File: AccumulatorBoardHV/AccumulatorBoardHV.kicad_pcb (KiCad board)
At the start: 2 copper layers, 42 parts, among them J1 TS -> GLV Regulator Jumper, J2 To LV Board, J3 Batt Voltage, J4 TS (Switched), J5 IMD TS, J6 To LV Board, J7 Acc LED 1, J8 Acc LED 2, J9 Charger Current, U1 V110C12E100BL, U2 DK1A1B-12V, U3 RDD08110S3V3, U4 PS2501-4, U5 G2RL-1A-E, U6 G2RL-1A-E

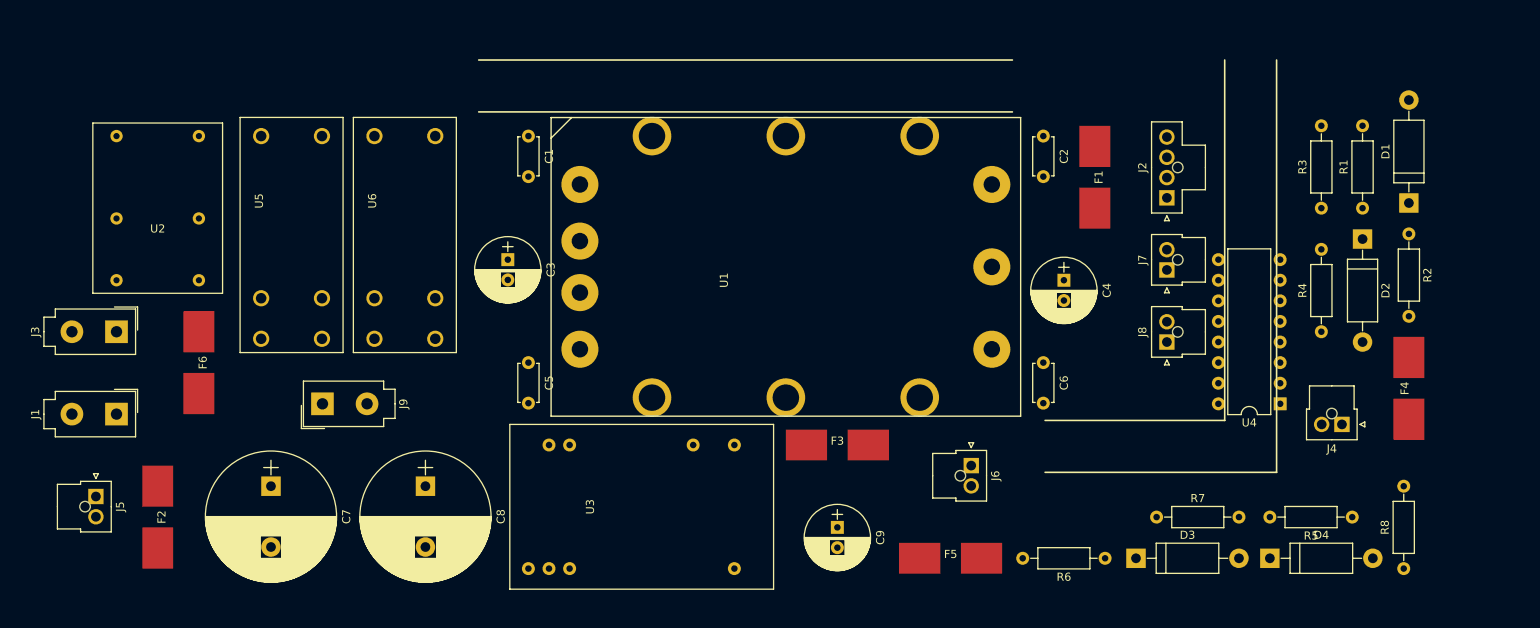
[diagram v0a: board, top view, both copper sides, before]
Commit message: Work for preparation for autorouting
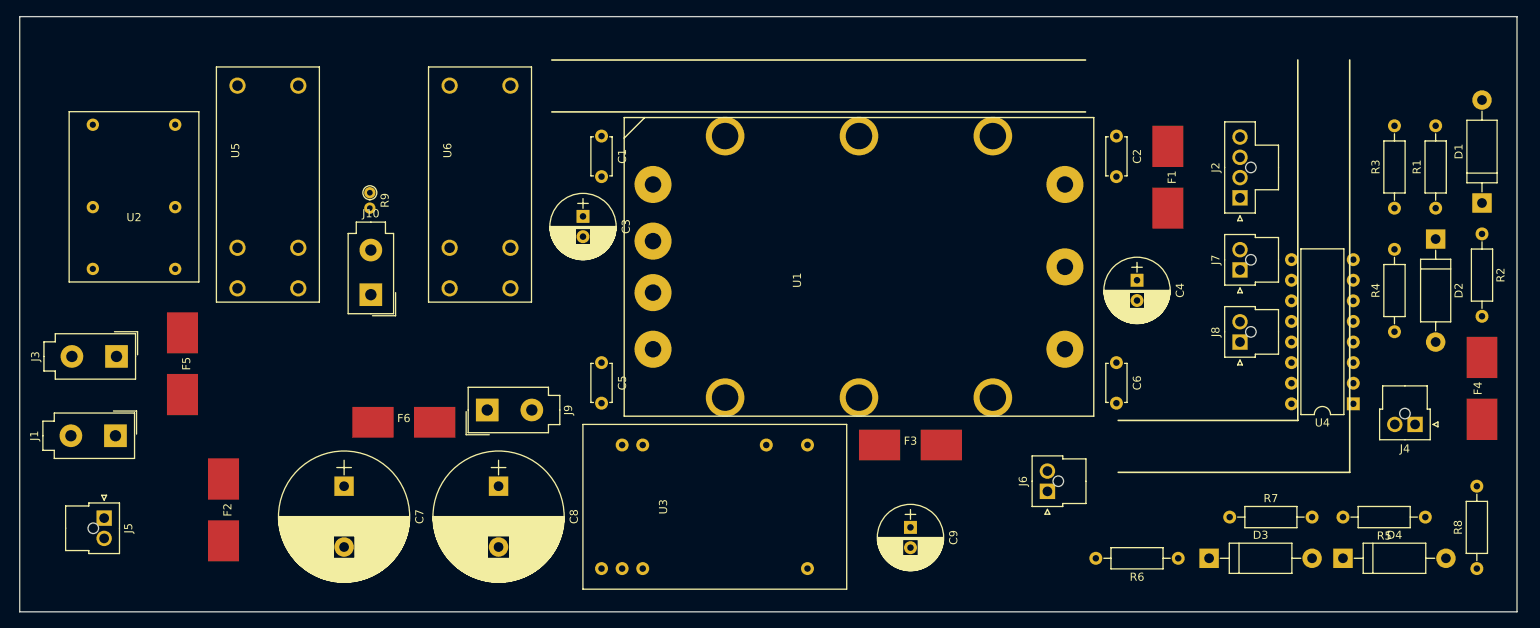
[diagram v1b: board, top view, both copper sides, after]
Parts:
- added J10: Charger Current, Connectors_Molex:Molex_MiniFit-JR-5556-02A_2x01x4.20mm_Straight, F.Cu at (61.8, 62.7)
- added R9: 0, Resistors_THT:R_Axial_DIN0204_L3.6mm_D1.6mm_P1.90mm_Vertical, F.Cu at (61.7, 50.2)
- J9: value Charger Current -> Charger Current to Batt
- moved F5 97.7 mm to (38.6, 71.2), turned to 90 degrees
- moved F6 26.3 mm to (65.9, 78.5), turned to 180 degrees
- moved J9 20.3 mm to (76.2, 77.0)
- moved U6 11.2 mm to (75.3, 37.0)
- moved C3 10.7 mm to (88.0, 53.1)
- moved J6 9.92 mm to (145.3, 87.0), turned to 90 degrees
- moved R8 9.02 mm to (198.2, 96.5)
- moved U1 9.02 mm to (96.6, 43.2)
- moved C1 9.02 mm to (90.3, 43.2)
- moved C2 9.02 mm to (153.8, 43.2)
- moved C4 9.02 mm to (156.3, 61.0)
- moved C5 9.02 mm to (90.3, 71.1)
- moved C6 9.02 mm to (153.8, 71.1)
- moved C7 9.02 mm to (58.5, 86.4)
- moved C8 9.02 mm to (77.6, 86.4)
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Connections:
- net Net-(F6-Pad2) renamed /BATT+_CHGFUSED
- F6 pad 1: /BATT+_DIRECT -> /BATT+_CHARGER
- J9 pad 1: /CHARGER+ -> /BATT+_CHARGER
- J9 pad 2: /CHARGER- -> /BATT-_CHARGER
- R8 pad 2: /CHARGER- -> Net-(R8-Pad2)
- U6 pad 3: /BATT- -> /BATT-_CHARGER
- U6 pad 5: /BATT- -> /BATT-_CHARGER
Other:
- board outline added: 184.7 x 73.4 mm
- net class BattCurrent added: clearance 0.2, trace_width 0.5, via_dia 1.2, via_drill 0.4
- net class ChgCurrent added: clearance 0.2, trace_width 4, via_dia 3.2, via_drill 2

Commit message: Autoroute AccumulatorHV PCB
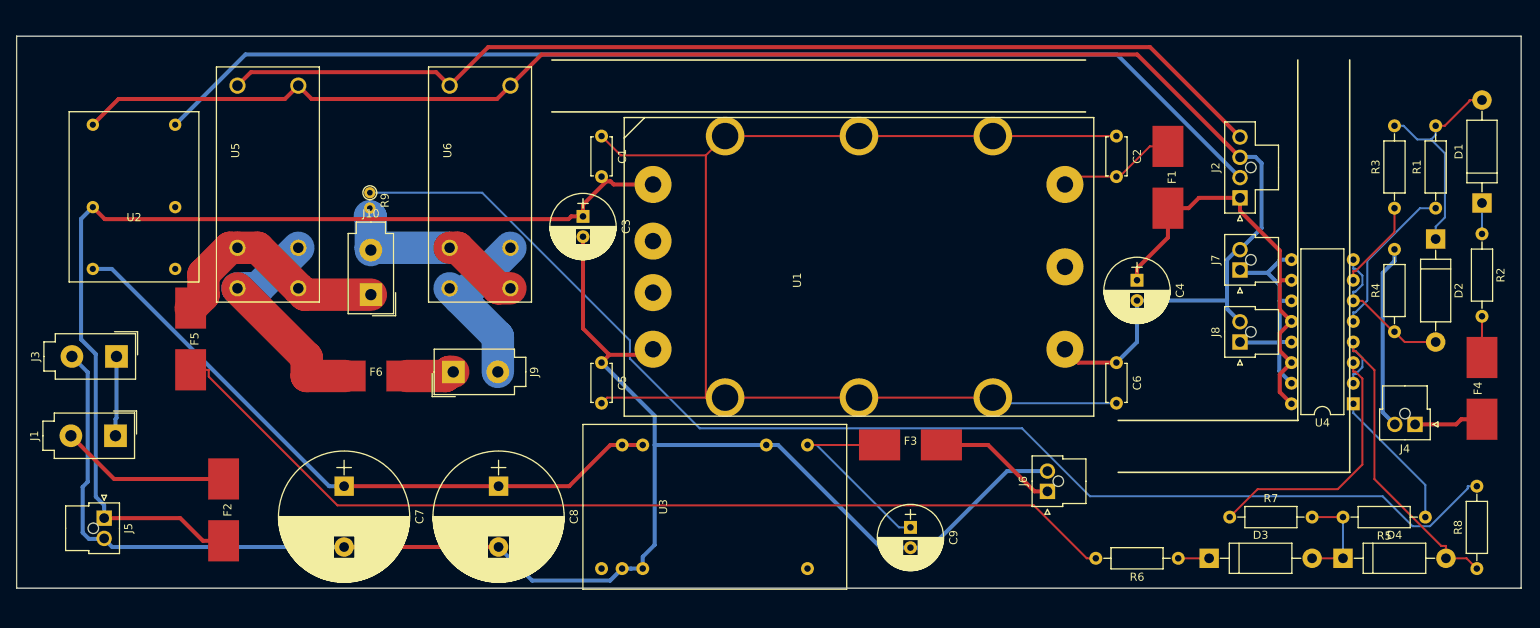
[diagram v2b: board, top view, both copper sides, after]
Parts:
- moved F6 6.66 mm to (62.5, 72.8)
- moved J9 6.30 mm to (72.0, 72.3)
- moved F5 3.21 mm to (39.6, 68.2)
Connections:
- net Net-(F2-Pad2) renamed /BATT+_DIRFUSED
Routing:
- net /BATT-: track 0.00 -> 204.3 mm
- net GND: track 0.00 -> 203.7 mm
- net Net-(C1-Pad1): track 0.00 -> 159.4 mm
- net Net-(R8-Pad2): track 0.00 -> 157.1 mm
- net /12V: track 0.00 -> 141.2 mm
- net /AIRS_FINAL_CHARGER: track 0.00 -> 131.6 mm
- net /BATT+: track 0.00 -> 129.5 mm
- net Net-(F5-Pad1): track 0.00 -> 121.7 mm
- net /BATT+_LVBOARD: track 0.00 -> 81.0 mm
- net /12V_SRC: track 0.00 -> 51.8 mm
- net Net-(D4-Pad2): track 0.00 -> 42.6 mm
- net Net-(R7-Pad1): track 0.00 -> 32.2 mm
- net /12V_INDICATOR: track 0.00 -> 29.9 mm
- net /CHARGER+: track 0.00 -> 29.2 mm
- net /BATT+_CHGFUSED: track 0.00 -> 28.7 mm
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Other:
- board size 184.7 x 73.4 mm -> 185.5 x 68.1 mm
- net class BattCurrent: clearance 0.2 -> 0.4
- net class Default: via_dia 0.6 -> 0.8

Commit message: Revise Accumulator HV and LV, route Dash Switchbox, begin PE HV
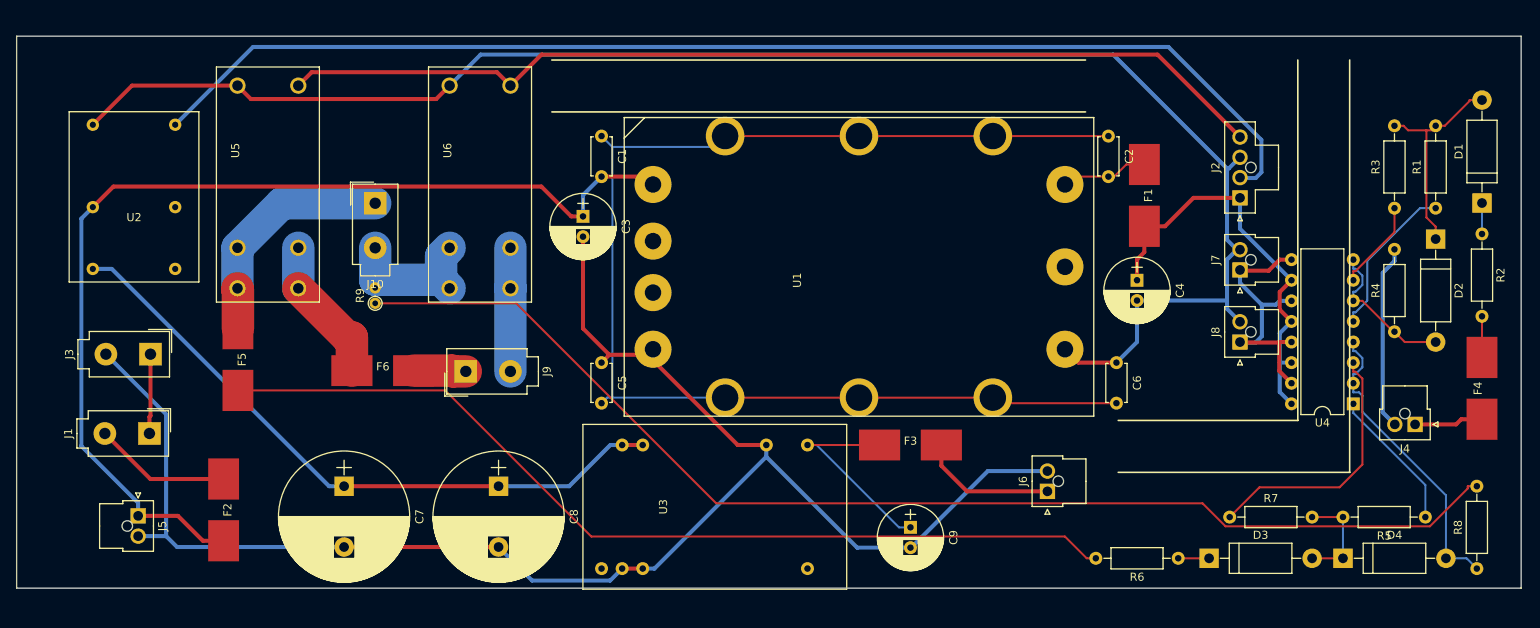
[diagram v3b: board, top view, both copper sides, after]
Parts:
- moved R9 13.7 mm to (62.4, 63.8), turned to 90 degrees
- moved J10 11.3 mm to (62.4, 51.5), turned to 0 degrees
- moved F5 6.36 mm to (45.5, 70.7)
- moved J3 4.20 mm to (34.7, 70.1)
- moved J5 4.20 mm to (33.1, 90.0)
- moved J1 4.20 mm to (34.5, 79.9)
- moved F1 3.67 mm to (157.2, 50.5)
- moved J9 1.55 mm to (73.6, 72.2)
- moved F6 1.07 mm to (63.3, 72.1)
- moved C2 0.99 mm to (152.8, 43.2)
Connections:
- U5 pad 1: GND -> /AIRS_FINAL_CHARGER
- U5 pad 4: /CHARGER+ -> /BATT+_CHGFUSED
- U5 pad 5: /BATT+_CHGFUSED -> /CHARGER+
- U5 pad 8: /AIRS_FINAL_CHARGER -> GND
- U6 pad 1: GND -> /AIRS_FINAL_CHARGER
- U6 pad 4: /CHARGER- -> /BATT-_CHARGER
- U6 pad 5: /BATT-_CHARGER -> /CHARGER-
- U6 pad 8: /AIRS_FINAL_CHARGER -> GND
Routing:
- net /BATT+_CHGFUSED: track 28.7 -> 18.2 mm
- net /12V: track 141.2 -> 149.6 mm
- net /AIRS_FINAL_CHARGER: track 131.6 -> 123.3 mm
- net Net-(R8-Pad2): track 157.1 -> 149.5 mm
- net Net-(F5-Pad1): track 121.7 -> 114.4 mm
- net /BATT-_CHARGER: track 21.6 -> 15.2 mm
- net /BATT-: track 204.3 -> 198.5 mm
- net /CHARGER-: track 24.5 -> 18.9 mm
- net /12V_INDICATOR: track 29.9 -> 35.2 mm
- net Net-(D4-Pad2): track 42.6 -> 37.4 mm
- net /BATT+_DIRFUSED: track 21.0 -> 17.0 mm
- net Net-(C2-Pad2): track 14.6 -> 10.8 mm
- net GND: track 203.7 -> 200.6 mm
- net /3.3V_TS: track 15.4 -> 16.9 mm
- net Net-(D1-Pad2): track 27.7 -> 26.9 mm
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
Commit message: Tweak AccumulatorHV PCB
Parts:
- moved F1 6.91 mm to (163.2, 47.0)
- moved C4 3.53 mm to (158.5, 58.2)
- moved J6 0.89 mm to (144.4, 87.0)
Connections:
- C2 pad 2: Net-(C2-Pad2) -> /VICOR_OUT
- C4 pad 1: /12V_SRC -> /VICOR_OUT
- F1 pad 2: Net-(C2-Pad2) -> /VICOR_OUT
- U1 pad 7: Net-(C2-Pad2) -> /VICOR_OUT
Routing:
- net /VICOR_OUT: track 0.00 -> 29.4 mm
- net /12V_SRC: track 52.2 -> 38.0 mm
- net Net-(C2-Pad2): track 10.8 -> 0.00 mm
- net /12V_INDICATOR: track 35.2 -> 29.9 mm
- net /BATT-: track 198.5 -> 196.6 mm
- net /3.3V_TS: track 16.9 -> 16.1 mm
- net GND: track 200.6 -> 201.2 mm

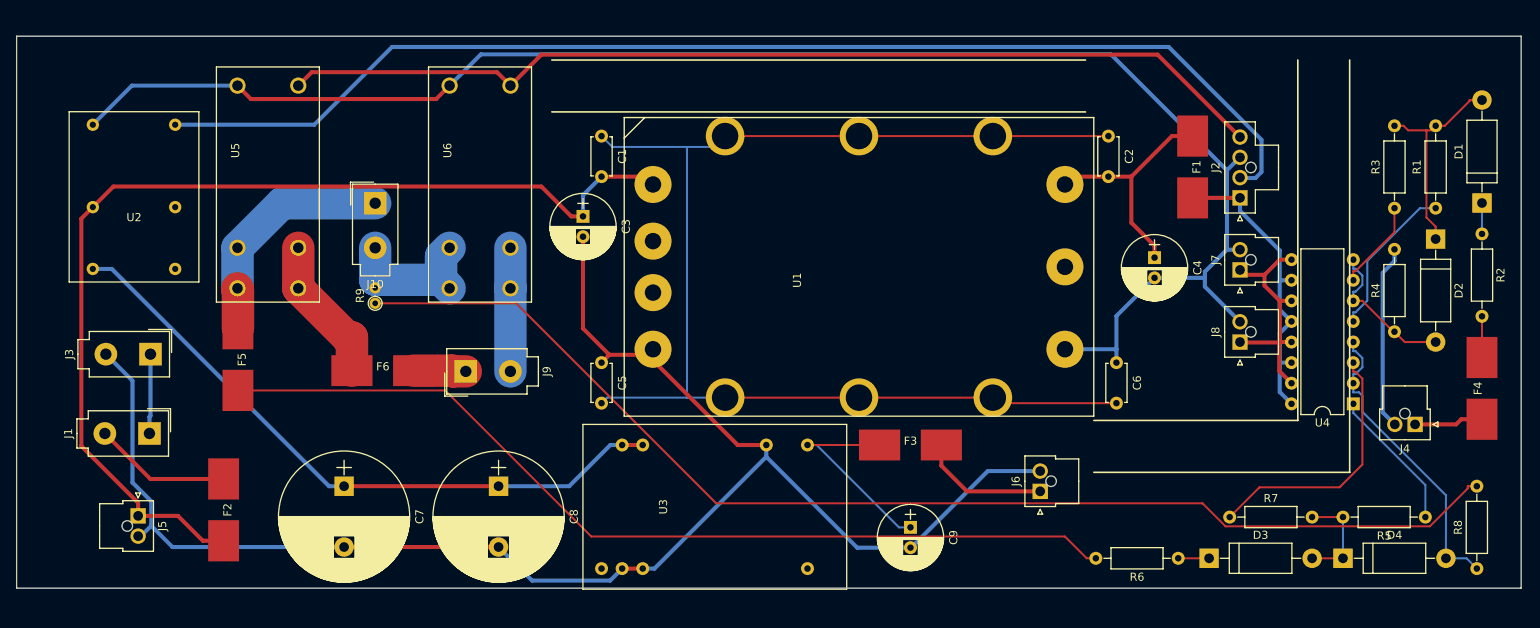
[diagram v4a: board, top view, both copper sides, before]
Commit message: Add mounting holes to Accumulator HV PCB
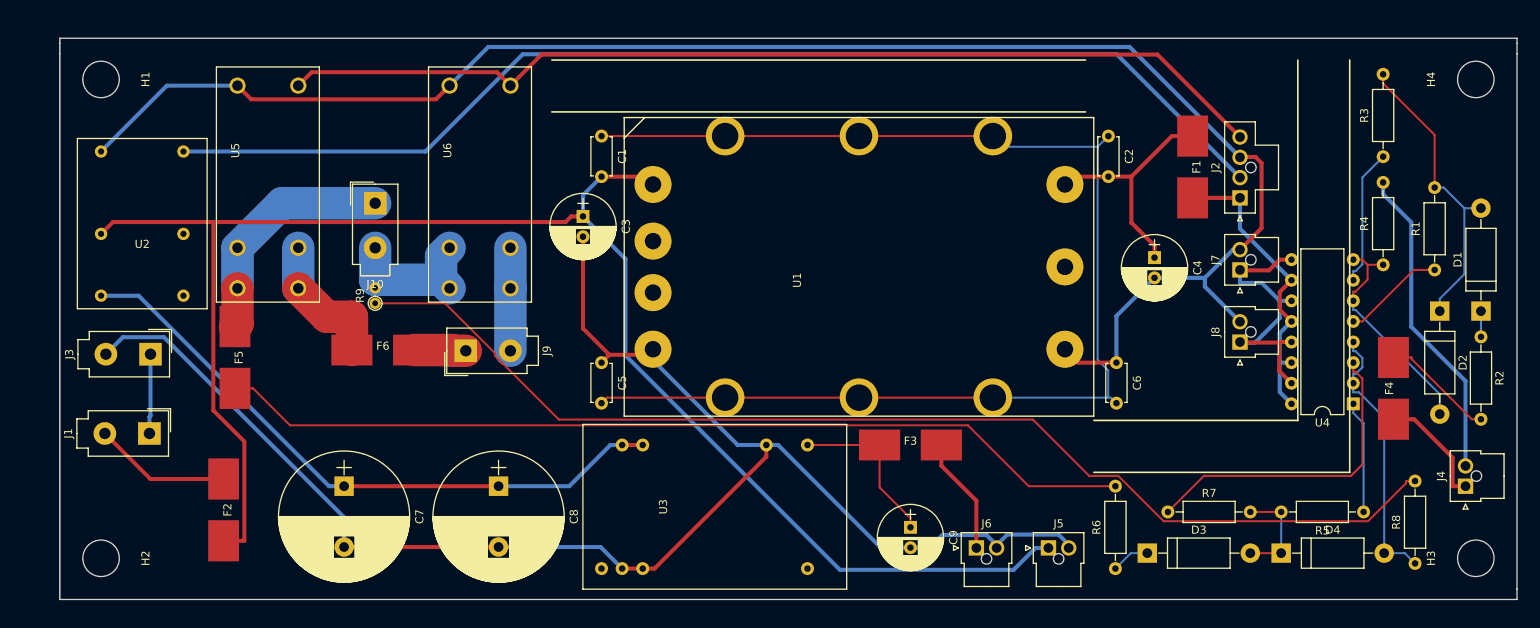
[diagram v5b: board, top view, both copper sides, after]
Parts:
- added H1: MtngHole, Mounting_Holes:MountingHole_4.5mm, F.Cu at (28.6, 36.2)
- added H2: MtngHole, Mounting_Holes:MountingHole_4.5mm, F.Cu at (28.6, 95.2)
- added H3: MtngHole, Mounting_Holes:MountingHole_4.5mm, F.Cu at (198.1, 95.2)
- added H4: MtngHole, Mounting_Holes:MountingHole_4.5mm, F.Cu at (198.1, 36.2)
- moved J5 112.3 mm to (145.4, 94.0), turned to 0 degrees
- moved D1 13.3 mm to (198.8, 64.8)
- moved R2 12.7 mm to (198.8, 67.9)
- moved F4 10.9 mm to (188.0, 74.3)
- moved J6 10.5 mm to (136.5, 94.0), turned to 0 degrees
- moved J4 9.84 mm to (196.8, 86.4), turned to 90 degrees
- moved D2 8.90 mm to (193.7, 64.8)
- moved R4 8.37 mm to (186.7, 59.1)
- moved R6 7.85 mm to (153.7, 96.5), turned to 90 degrees
- moved D3 7.65 mm to (157.6, 94.6)
- moved D4 7.65 mm to (174.1, 94.6)
- moved R5 7.65 mm to (184.3, 89.5)
- moved R7 7.65 mm to (160.1, 89.5)
- moved R8 7.65 mm to (190.6, 95.9)
- moved R1 7.62 mm to (193.0, 59.7)
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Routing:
- net /BATT+: track 129.0 -> 199.9 mm
- net /TS-: track 22.8 -> 39.2 mm
- net Net-(D1-Pad2): track 26.9 -> 37.3 mm
- net Net-(D2-Pad2): track 18.6 -> 27.8 mm
- net Net-(F4-Pad1): track 5.08 -> 14.1 mm
- net /12V: track 149.6 -> 141.6 mm
- net Net-(R8-Pad2): track 149.5 -> 141.8 mm
- net Net-(R7-Pad1): track 32.2 -> 39.6 mm
- net Net-(R1-Pad1): track 19.5 -> 12.7 mm
- net /12V_INDICATOR: track 29.9 -> 36.1 mm
- net /TS+: track 8.52 -> 14.4 mm
- net Net-(R3-Pad1): track 11.2 -> 16.9 mm
- net Net-(C9-Pad1): track 25.8 -> 20.6 mm
- net GND: track 201.2 -> 206.2 mm
- net /BATT-: track 196.6 -> 191.6 mm
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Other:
- board size 185.5 x 68.1 mm -> 179.7 x 69.2 mm

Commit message: Add larger fuse to AccumulatorHV board
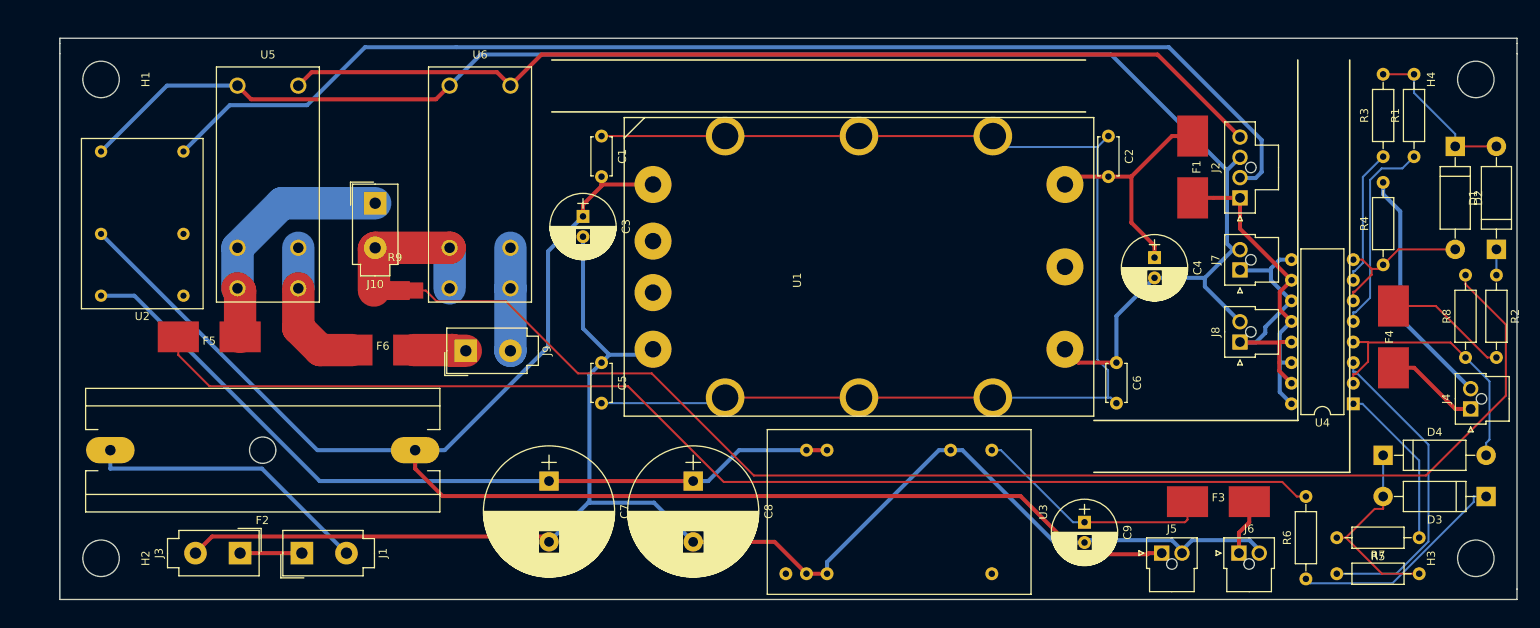
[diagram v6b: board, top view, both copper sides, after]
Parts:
- F2: footprint FSFootprints:SMD Fuse -> Fuse_Holders_and_Fuses:Fuseholder6x32_Horiz_Open_Schurter0031-8002
- R9: footprint Resistors_THT:R_Axial_DIN0204_L3.6mm_D1.6mm_P1.90mm_Vertical -> Oddities:NetTie-I_Connected_SMD
- moved D3 42.4 mm to (199.4, 87.6), turned to 180 degrees
- moved F3 38.6 mm to (166.4, 88.3)
- moved J6 32.4 mm to (168.9, 94.6)
- moved J3 26.9 mm to (45.7, 94.6)
- moved R8 26.2 mm to (196.8, 70.5)
- moved C7 25.3 mm to (83.8, 85.7)
- moved F2 24.7 mm to (67.3, 81.9), turned to 180 degrees
- moved C8 24.0 mm to (101.6, 85.7)
- moved J1 23.9 mm to (53.3, 94.6), turned to 90 degrees
- moved R6 23.5 mm to (177.2, 97.8)
- moved U3 22.7 mm to (113.0, 97.2)
- moved R7 22.2 mm to (181.0, 97.2)
- moved C9 21.5 mm to (149.9, 90.8)
- moved D2 20.4 mm to (195.6, 44.5)
- moved D4 17.4 mm to (186.7, 82.5)
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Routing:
- net Net-(F5-Pad1): track 113.6 -> 148.5 mm
- net Net-(R8-Pad2): track 141.8 -> 165.0 mm
- net Net-(D3-Pad1): track 4.73 -> 27.3 mm
- net /BATT+_LVBOARD: track 78.6 -> 100.6 mm
- net /BATT+_DIRFUSED: track 17.0 -> 35.7 mm
- net Net-(D1-Pad2): track 37.3 -> 19.9 mm
- net Net-(R1-Pad1): track 12.7 -> 25.1 mm
- net Net-(D3-Pad2): track 12.7 -> 24.7 mm
- net Net-(C9-Pad1): track 20.6 -> 30.2 mm
- net /TS-: track 39.2 -> 29.9 mm
- net Net-(D2-Pad2): track 27.8 -> 19.0 mm
- net /12V: track 141.6 -> 150.0 mm
- net /3.3V_TS: track 14.5 -> 6.88 mm
- net Net-(R5-Pad1): track 13.9 -> 20.5 mm
- net GND: track 206.2 -> 202.1 mm
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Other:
- net class BattCurrent: via_drill 0.4 -> 0.6
